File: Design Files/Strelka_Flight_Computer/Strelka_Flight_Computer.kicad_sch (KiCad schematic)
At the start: 10 parts

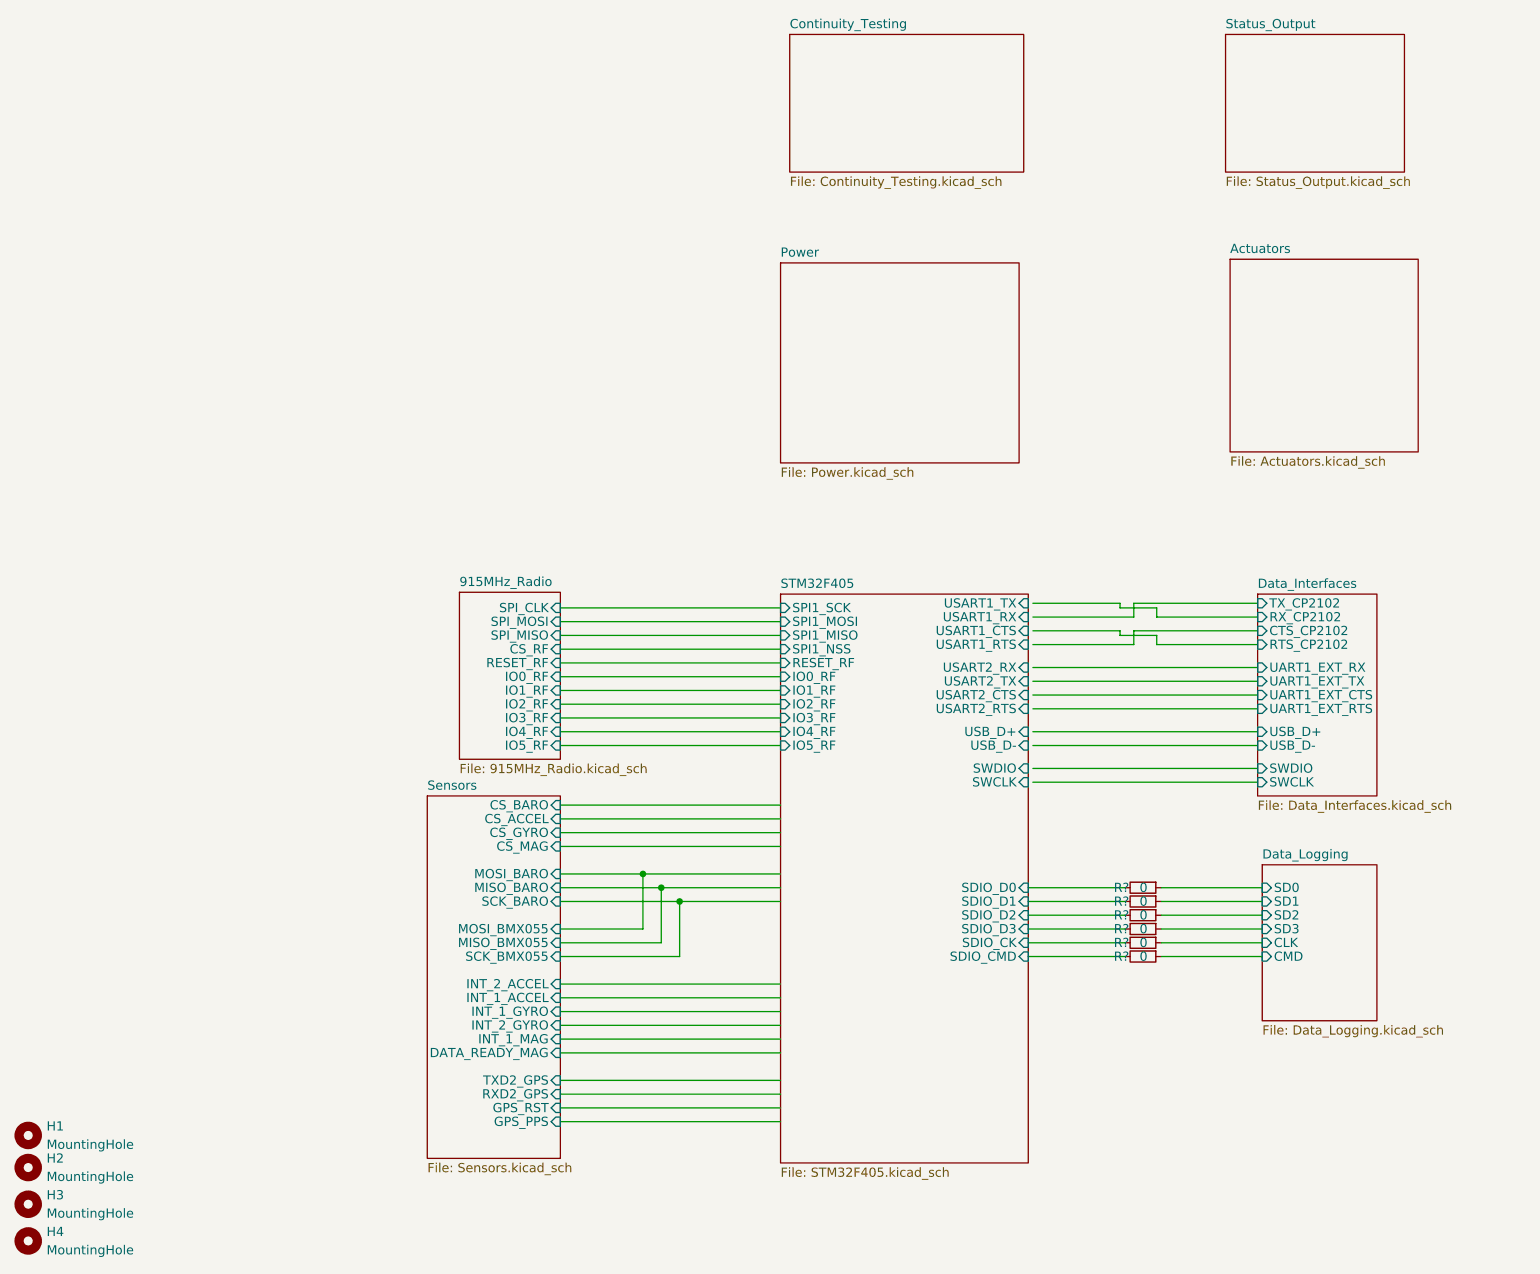
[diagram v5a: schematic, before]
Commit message: Pin mapping and created STM32 .ioc for reference
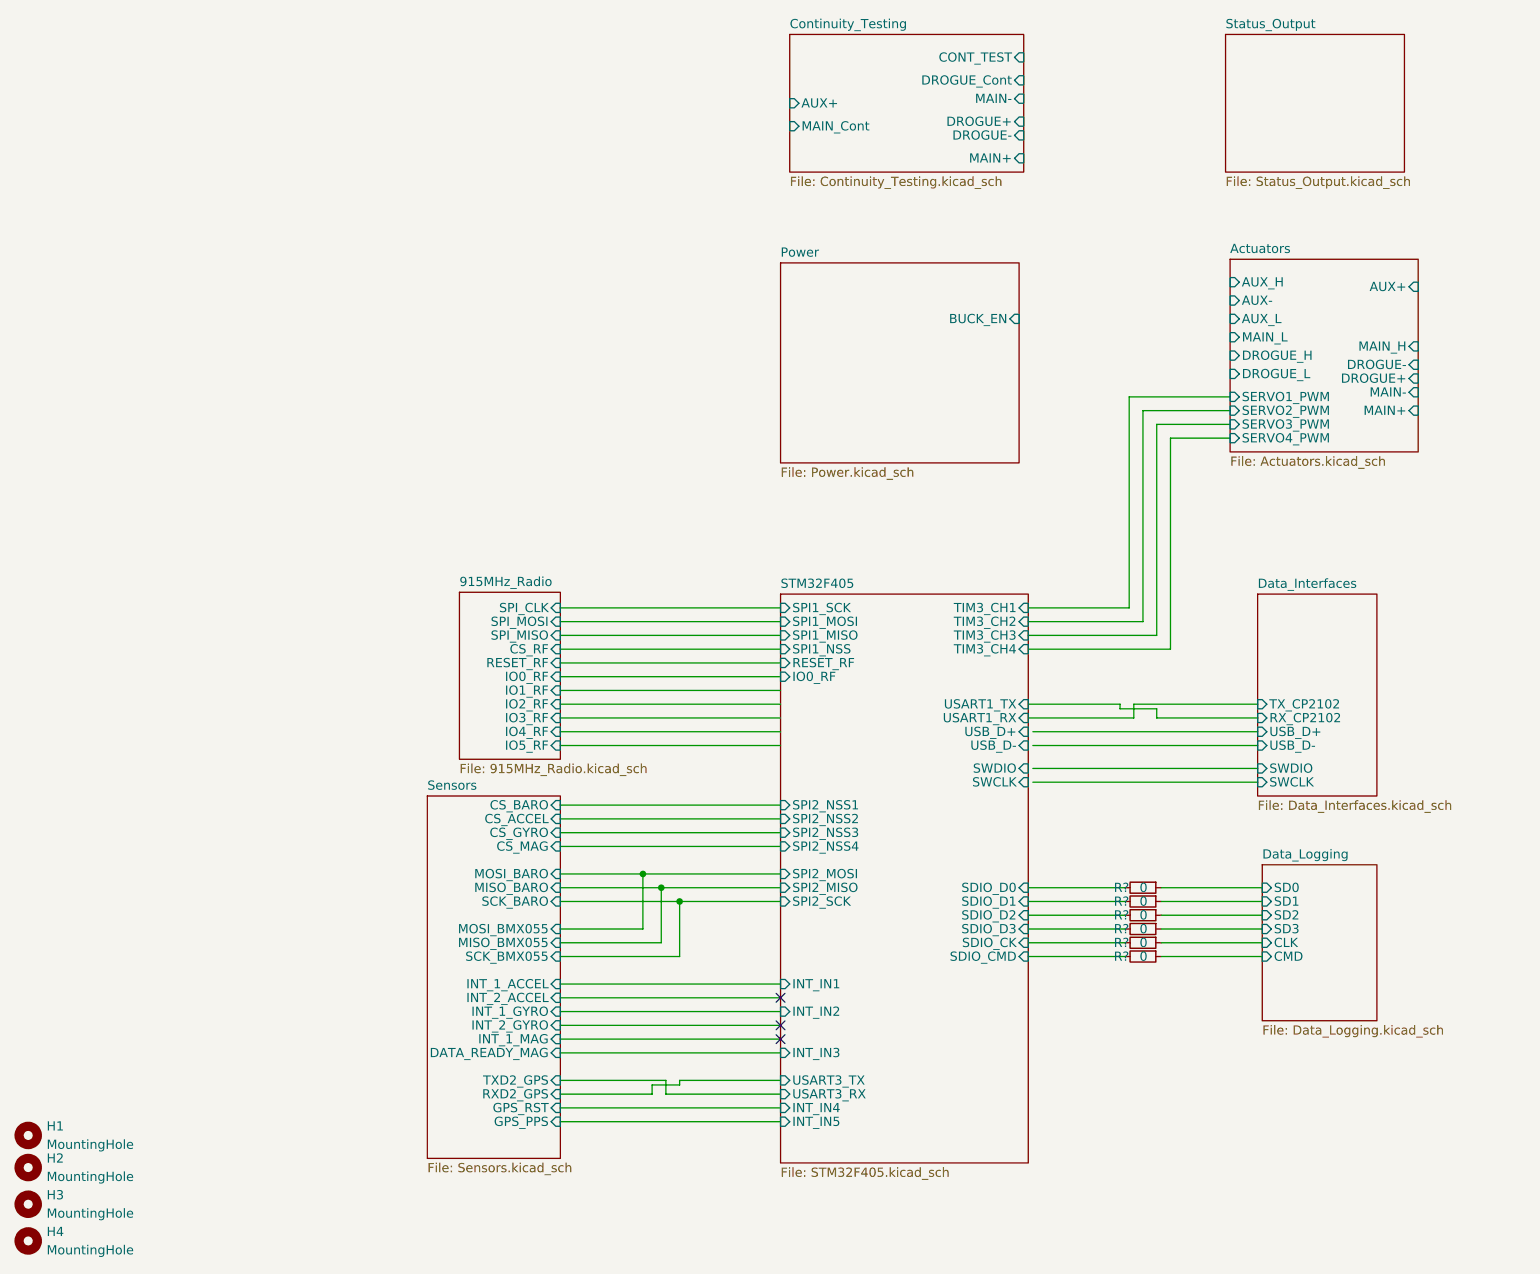
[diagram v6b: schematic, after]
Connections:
- no-connect marks 0 -> 3
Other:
- sheet Actuators ports: added AUX+, AUX-, AUX_H, AUX_L, DROGUE+, DROGUE-, DROGUE_H, DROGUE_L, MAIN+, MAIN-, MAIN_H, MAIN_L, SERVO1_PWM, SERVO2_PWM, SERVO3_PWM, SERVO4_PWM; removed none
- sheet Continuity_Testing ports: added AUX+, CONT_TEST, DROGUE+, DROGUE-, DROGUE_Cont, MAIN+, MAIN-, MAIN_Cont; removed none
- sheet Data_Interfaces ports: added none; removed CTS_CP2102, RTS_CP2102, UART1_EXT_CTS, UART1_EXT_RTS, UART1_EXT_RX, UART1_EXT_TX
- sheet Power ports: added BUCK_EN; removed none
- sheet STM32F405 ports: added INT_IN1, INT_IN2, INT_IN3, INT_IN4, INT_IN5, SPI2_MISO, SPI2_MOSI, SPI2_NSS1, SPI2_NSS2, SPI2_NSS3, SPI2_NSS4, SPI2_SCK, TIM3_CH1, TIM3_CH2, TIM3_CH3, TIM3_CH4, USART3_RX, USART3_TX; removed IO1_RF, IO2_RF, IO3_RF, IO4_RF, IO5_RF, USART1_CTS, USART1_RTS, USART2_CTS, USART2_RTS, USART2_RX, USART2_TX
